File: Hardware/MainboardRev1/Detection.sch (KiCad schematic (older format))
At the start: 16 parts, among them J10 Switch_3, J11 Switch_2, J12 Switch_4, J9 Switch_1

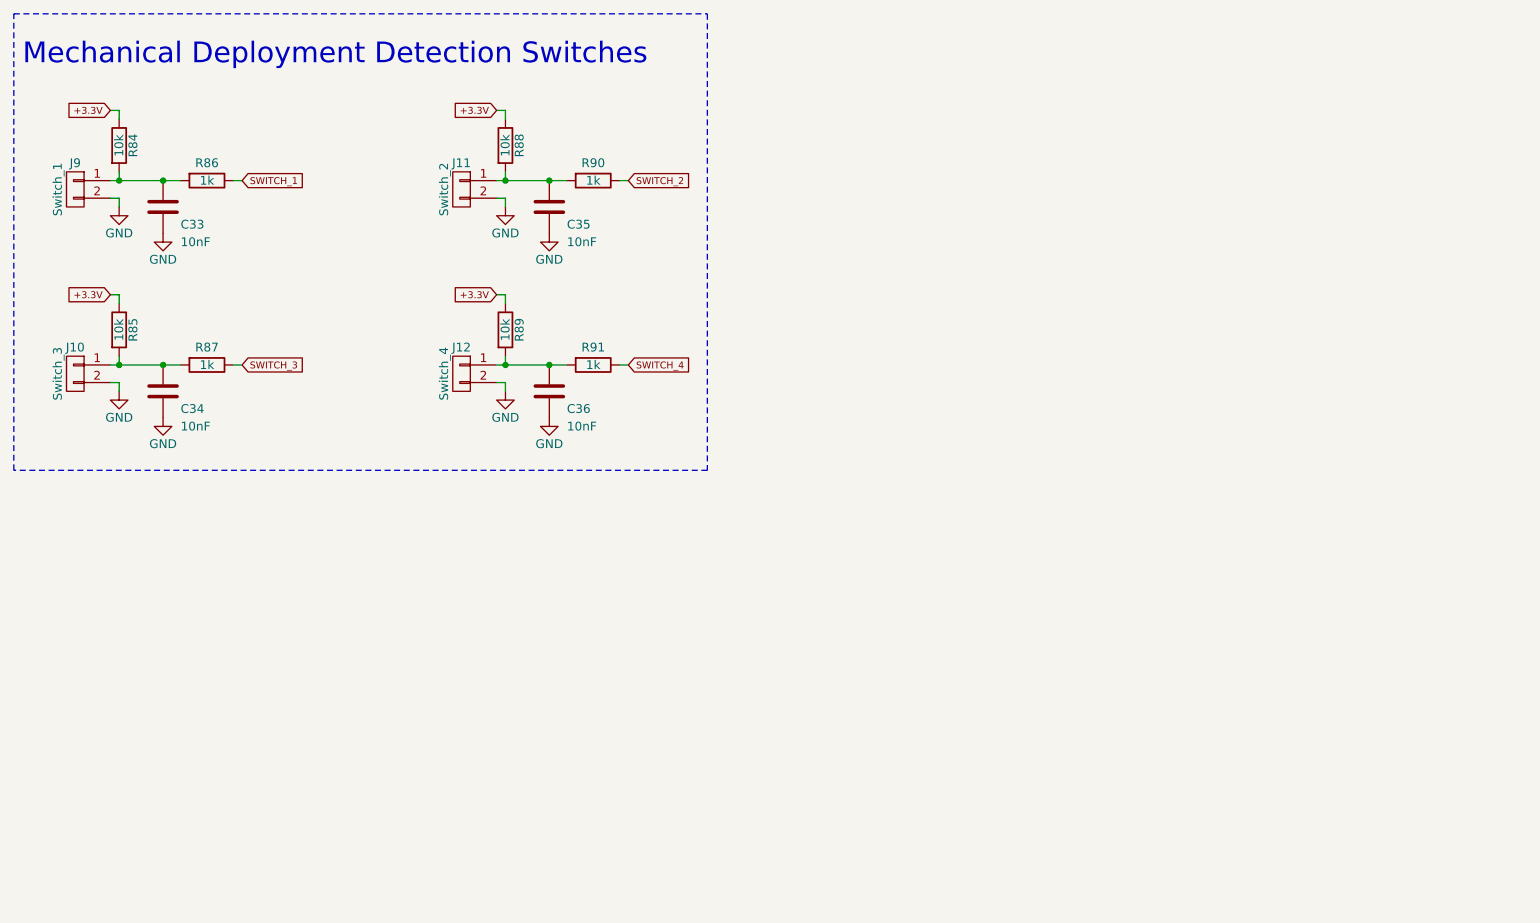
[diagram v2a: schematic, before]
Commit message: Added buzzer and strobe LED. Created BOM. Reannotated. Added sponsors to silkscreen. Needs to be routed and sent out. Good luck Matt!
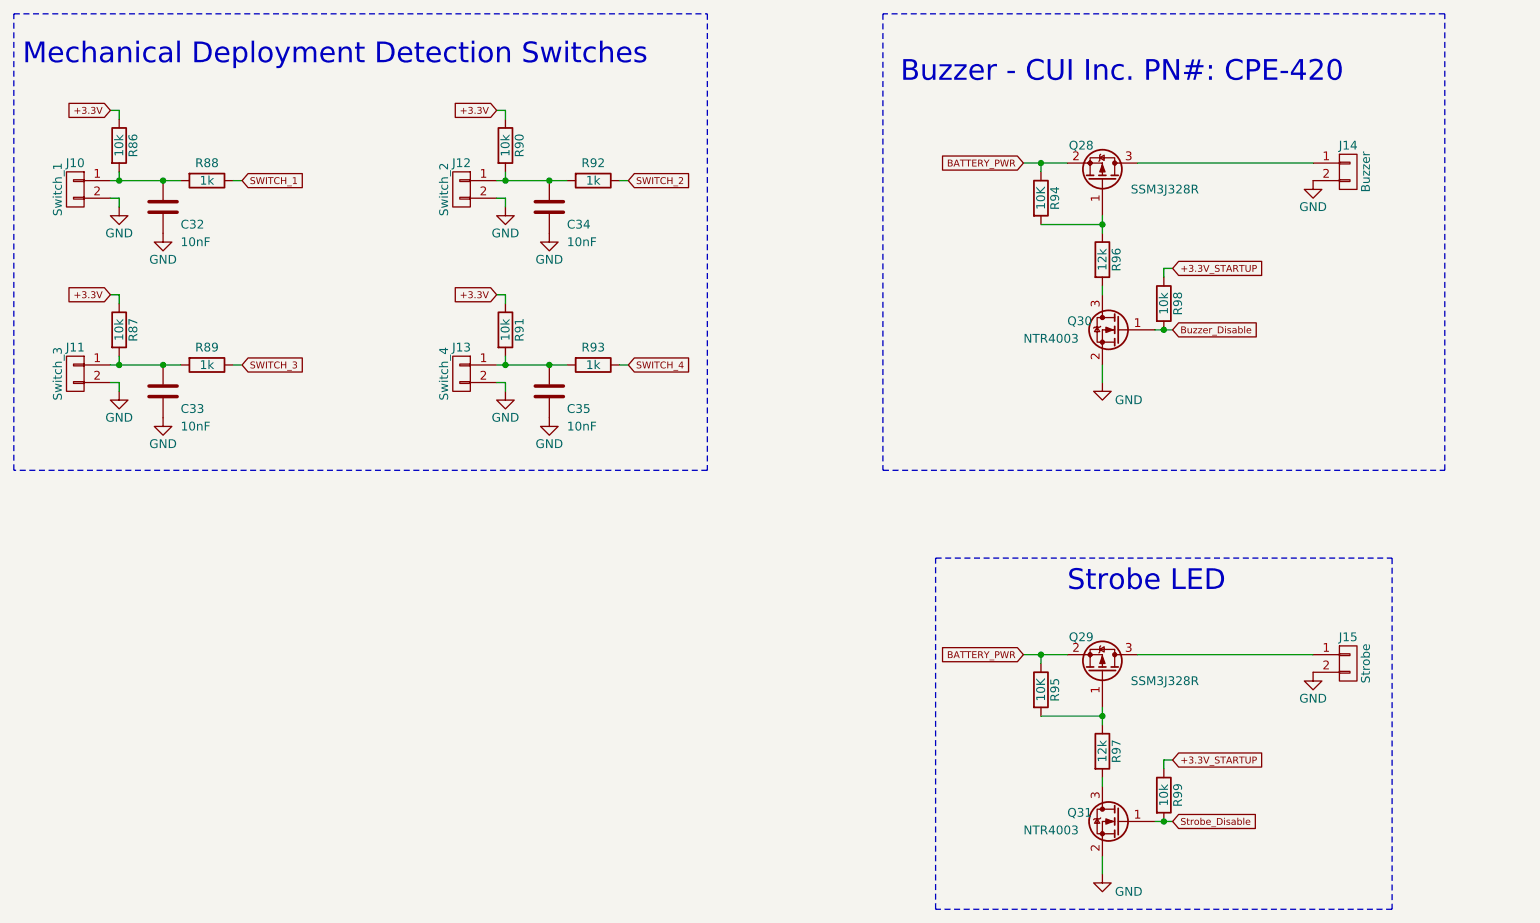
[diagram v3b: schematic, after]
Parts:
- added J14: Buzzer, Dans_Parts:CONN_2POS_VERT_TE_CONN_LOCK_5-103669-1, symbol CONN_01X02
- added J15: Strobe, Dans_Parts:CONN_2POS_VERT_TE_CONN_LOCK_5-103669-1, symbol CONN_01X02
- added Q28, Q29: SSM3J328R, TO_SOT_Packages_SMD:SOT-23, symbol Q_PMOS_GSD
- added Q30, Q31: NTR4003, TO_SOT_Packages_SMD:SOT-23, symbol Q_NMOS_GSD
- added R94, R95: 10K, Resistors_SMD:R_0603_HandSoldering, symbol R
- added R96, R97: 12k, Resistors_SMD:R_0603_HandSoldering, symbol R
- added R98, R99: 10k, Resistors_SMD:R_0603_HandSoldering, symbol R
- renumbered C33 to C32, C34 to C33, C35 to C34, C36 to C35, J9 to J10, J10 to J11, J11 to J12, J12 to J13, R84 to R86, R85 to R87, R86 to R88, R87 to R89, R88 to R90, R89 to R91, R90 to R92, R91 to R93
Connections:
- net GND: now also J14.2 (P2), J15.2 (P2), Q30.2 (S), Q31.2 (S)
- new net: J14.1 (P1), Q28.3 (D)
- new net: Q28.1 (G), R94.2, R96.1
- new net: Q30.3 (D), R96.2
- new net: J15.1 (P1), Q29.3 (D)
- new net: Q29.1 (G), R95.2, R97.1
- new net: Q31.3 (D), R97.2
- new net +3.3V_STARTUP: R98.1, R99.1
- new net BATTERY_PWR: Q28.2 (S), Q29.2 (S), R94.1, R95.1
- new net Buzzer_Disable: Q30.1 (G), R98.2
- new net Strobe_Disable: Q31.1 (G), R99.2
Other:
- note added: "Buzzer - CUI Inc. PN#: CPE-420"
- note added: "Strobe LED"
